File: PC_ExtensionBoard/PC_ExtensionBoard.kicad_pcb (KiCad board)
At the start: 2 copper layers, 135 x 125 mm, 2 parts, among them CN1 QT002206-4131-3H, CN2 QT002206-4131-3H

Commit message: update 3d
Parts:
- added CN3: HYC70-HDMIA19-230, DatCao_FootPrint:HDMI-TH_HYC70-HDMIA19-230, B.Cu at (89.5, 65.8)
- added DC1: DC-044A-20A, DatCao_FootPrint:DC-IN-TH_DC-044A-20A, B.Cu at (162.2, 56.8)
- added RJ1: 936273608, DatCao_FootPrint:RJ45-TH_936273608, B.Cu at (71.5, 64.0)
- added USB1: HC-USB3.0-L257-J, DatCao_FootPrint:USB-A-TH_HC-USB3.0-L257-J, B.Cu at (54.0, 68.6)
- added USB2: HC-USB2.0-L195-P, DatCao_FootPrint:USB-TH_73725-0110BLF, B.Cu at (99.2, 65.0)
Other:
- board size 135 x 125 mm -> 128.2 x 98.2 mm

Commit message: update footprint with 3D
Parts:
- removed CN3: HYC70-HDMIA19-230, DatCao_FootPrint:HDMI-TH_HYC70-HDMIA19-230
- removed USB2: HC-USB2.0-L195-P, DatCao_FootPrint:USB-TH_73725-0110BLF
- added HDMI1: HDMI-019S, ACLAB:HDMI-SMD_HDMI-019S, B.Cu at (107.5, 56.6)
- added PJ1: PJ-327A, ACLAB:AUDIO-IN-SMD_PJ-327A_C22355751, B.Cu at (164.3, 140.2)
- added U1: HC-USB3.0-L168-WP, ACLAB:USB-TH_USB3.0-A, B.Cu at (70.5, 62.1)
- added U2: 10GHz, ACLAB:SMA-TH_SMA-KWE, B.Cu at (56.5, 54.1)
- added USBC1: TYPE-C-31-M-12, ACLAB:USB-C_SMD-TYPE-C-31-M-12_1, B.Cu at (151.5, 141.5)
- CN1, CN2: footprint DatCao_FootPrint:CORE_BOARD_220PIN_Female -> ACLAB:CONN-SMD_QT002206-4131-3H
- DC1: footprint DatCao_FootPrint:DC-IN-TH_DC-044A-20A -> ACLAB:DC-IN-TH_DC-044A-20A
- RJ1: value 936273608 -> DS1128-09-S8B8S; footprint DatCao_FootPrint:RJ45-TH_936273608 -> ACLAB:RJ45-TH_DS1128-09-S8B8S
- USB1: value HC-USB3.0-L257-J -> HC-USB3.0-L175-2X1-P; footprint DatCao_FootPrint:USB-A-TH_HC-USB3.0-L257-J -> ACLAB:USB-A-TH_H181-AF2R06-12ALCR
- moved RJ1 56.4 mm to (127.8, 60.0), turned to 0 degrees
- moved USB1 36.3 mm to (89.5, 61.2)
- moved DC1 2.62 mm to (164.4, 55.3)

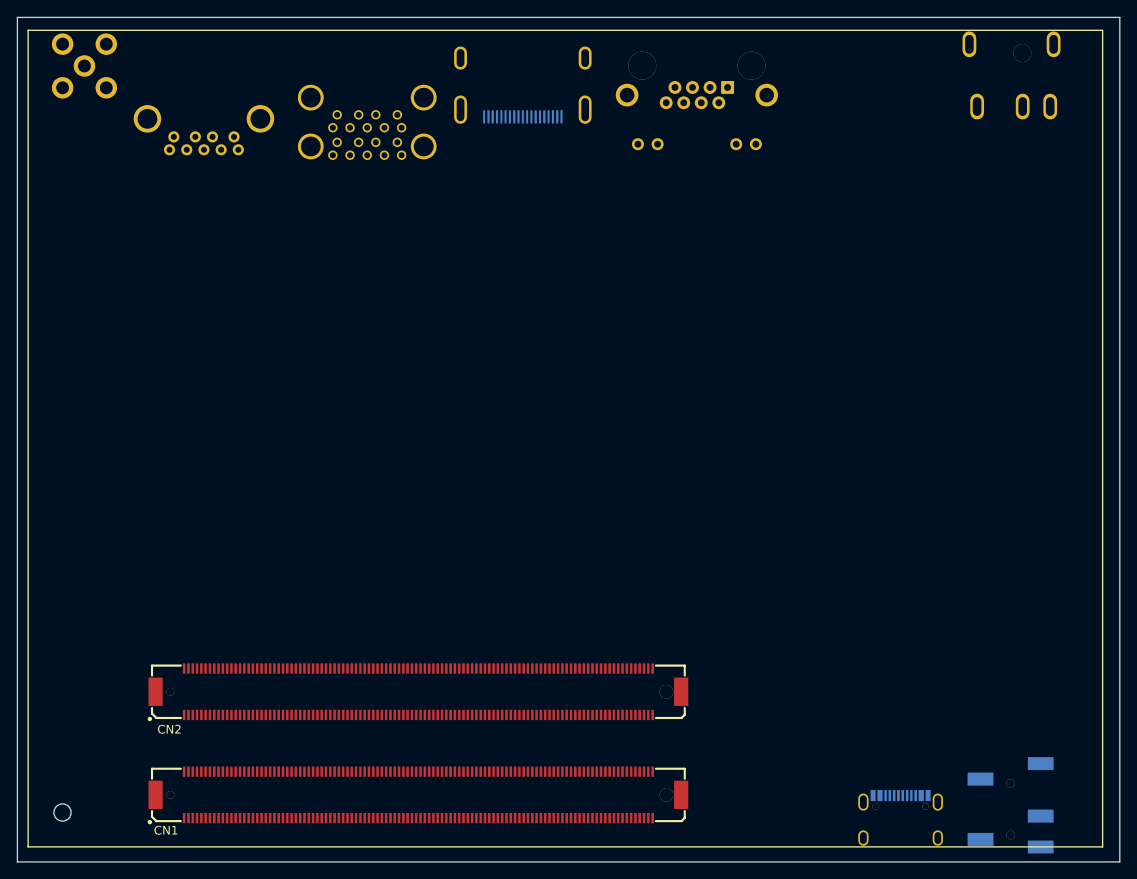
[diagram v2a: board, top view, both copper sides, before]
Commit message: finish 3D file for integration
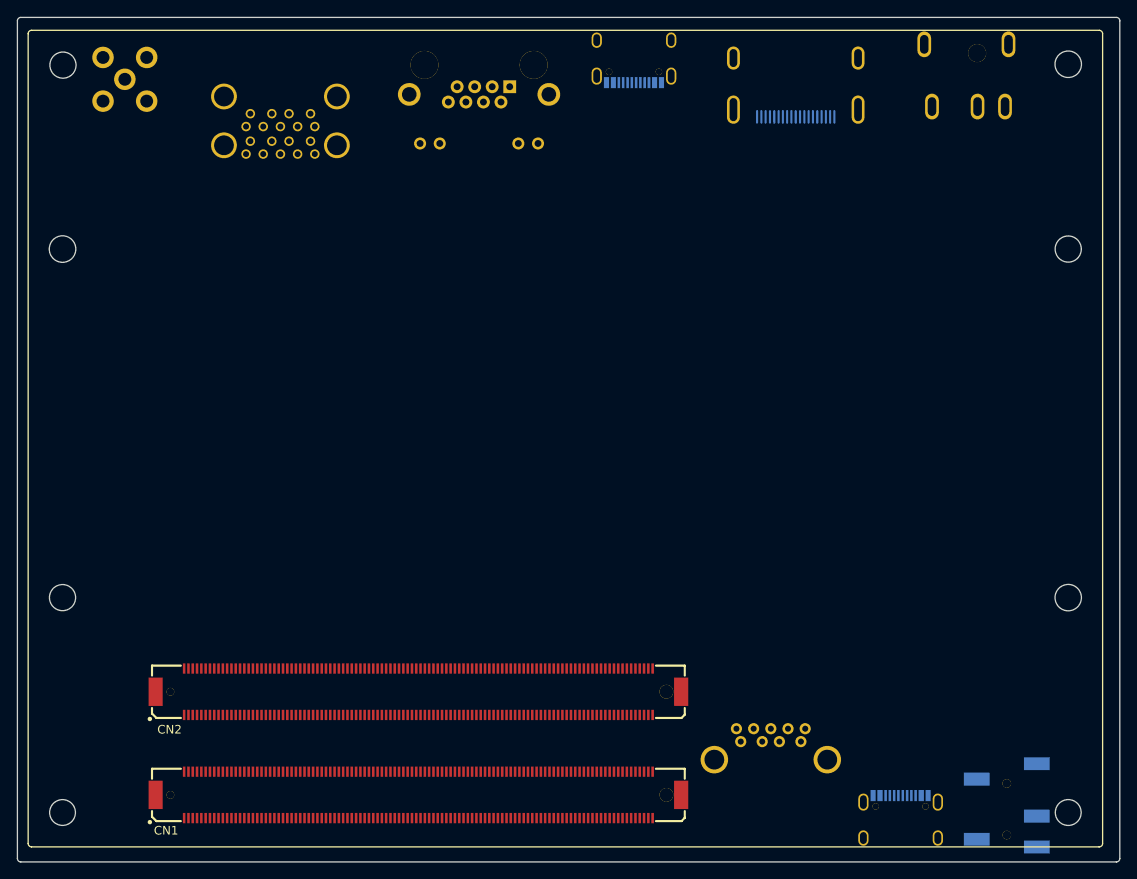
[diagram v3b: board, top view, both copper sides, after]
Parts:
- added USBC1: TYPE-C-31-M-12, ACLAB:USB-C_SMD-TYPE-C-31-M-12_1, B.Cu at (120.5, 53.6)
- moved U1 96.9 mm to (136.4, 133.1), turned to 180 degrees
- moved HDMI1 31.8 mm to (139.3, 56.6)
- moved RJ1 25.3 mm to (102.5, 59.9)
- moved USB1 10.1 mm to (79.3, 61.0)
- moved DC1 5.25 mm to (159.2, 55.3)
- moved U2 4.95 mm to (61.2, 55.7)
- moved PJ1 0.45 mm to (163.8, 140.2)
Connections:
- U1 pad 1: unconnected-(U1-VBUS-Pad1) -> (no net)
- U1 pad 10: unconnected-(U1-SH-Pad10) -> (no net)
- U1 pad 2: unconnected-(U1-D--Pad2) -> (no net)
- U1 pad 3: unconnected-(U1-D+-Pad3) -> (no net)
- U1 pad 4: unconnected-(U1-GND-Pad4) -> (no net)
- U1 pad 5: unconnected-(U1-SSRX--Pad5) -> (no net)
- U1 pad 6: unconnected-(U1-SSRX+-Pad6) -> (no net)
- U1 pad 7: unconnected-(U1-GND_DRAN-Pad7) -> (no net)
- U1 pad 8: unconnected-(U1-SSTX--Pad8) -> (no net)
- U1 pad 9: unconnected-(U1-SSTX+-Pad9) -> (no net)
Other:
- outline, holes or cut-outs redrawn

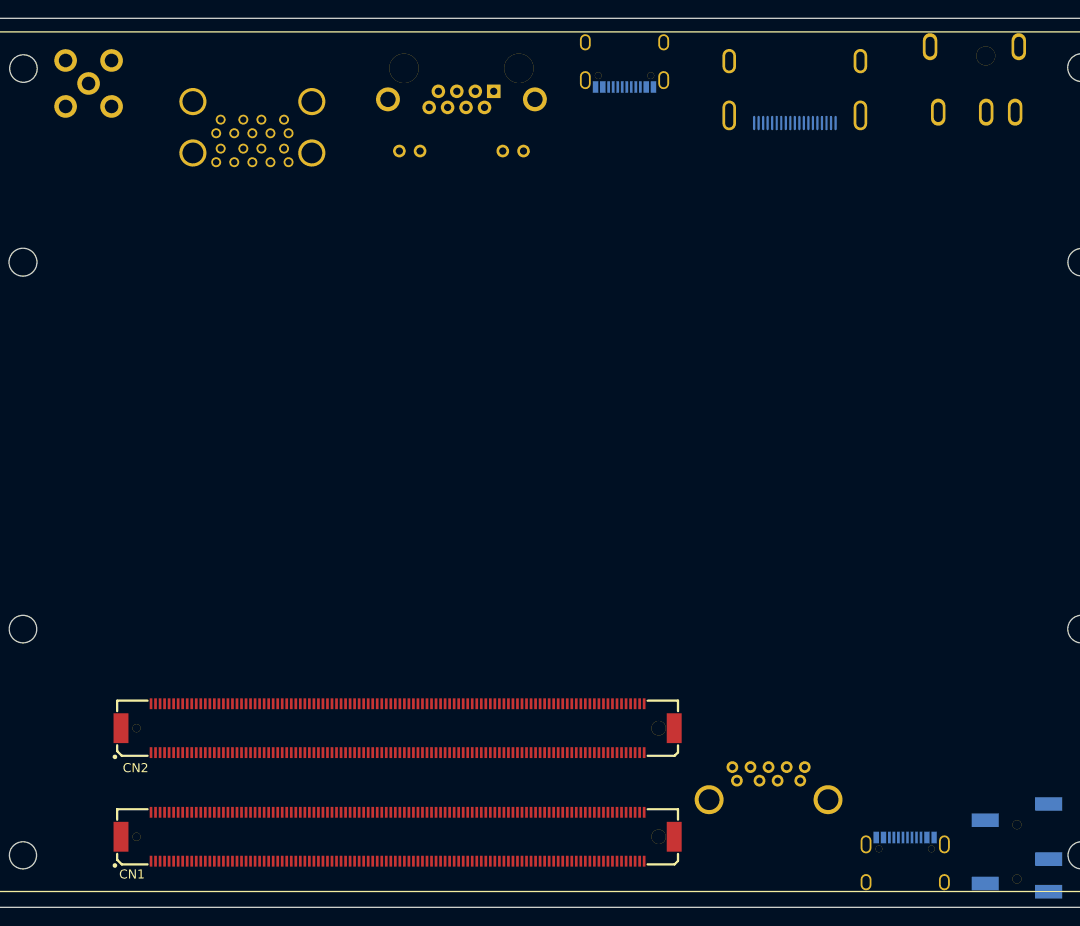
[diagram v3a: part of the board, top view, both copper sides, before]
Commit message: Update Symbol for Coreboard
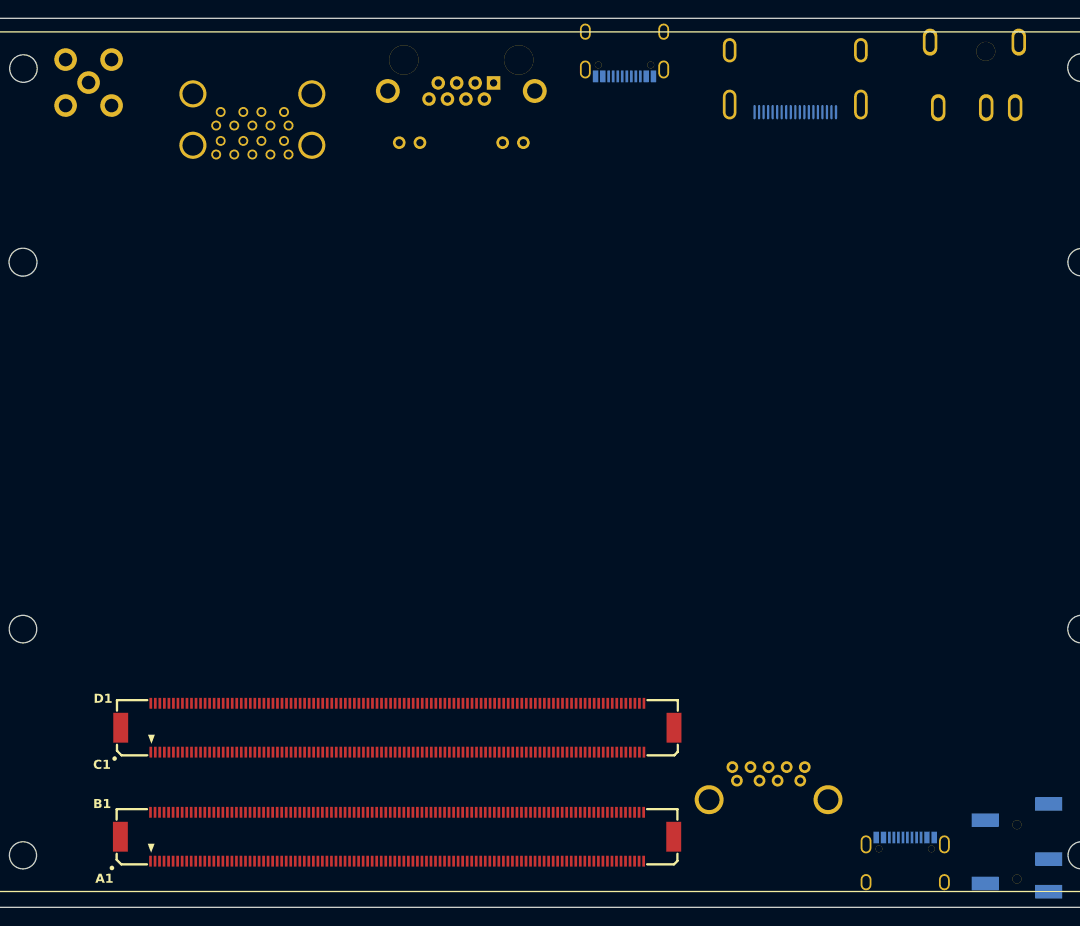
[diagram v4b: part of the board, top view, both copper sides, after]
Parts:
- removed CN1, CN2: QT002206-4131-3H, ACLAB:CONN-SMD_QT002206-4131-3H
- added U3: KBLH-E61_COMe_Type6_16U, DatCao_FootPrint:CORE_BOARD_CUSTOM_440_PIN, F.Cu at (95.3, 134.0)
- moved HDMI1 1.20 mm to (139.3, 55.5)
- moved USBC2 1.18 mm to (120.5, 52.4)
- moved RJ1 0.92 mm to (102.4, 58.9)
- moved USB1 0.85 mm to (79.3, 60.2)
- moved DC1 0.50 mm to (159.2, 54.8)
- moved U2 0.10 mm to (61.2, 55.6)
- renumbered USBC1 to USBC2
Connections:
- U1 pad 1: (no net) -> unconnected-(U1-VBUS-Pad1)
- U1 pad 10: (no net) -> unconnected-(U1-SH-Pad10)
- U1 pad 2: (no net) -> unconnected-(U1-D--Pad2)
- U1 pad 3: (no net) -> unconnected-(U1-D+-Pad3)
- U1 pad 4: (no net) -> unconnected-(U1-GND-Pad4)
- U1 pad 5: (no net) -> unconnected-(U1-SSRX--Pad5)
- U1 pad 6: (no net) -> unconnected-(U1-SSRX+-Pad6)
- U1 pad 7: (no net) -> unconnected-(U1-GND_DRAN-Pad7)
- U1 pad 8: (no net) -> unconnected-(U1-SSTX--Pad8)
- U1 pad 9: (no net) -> unconnected-(U1-SSTX+-Pad9)
- USB1 pad 1: unconnected-(USB1-VBUS-Pad1) -> /USB_Audio/P1_VBUS
- USB1 pad 10: unconnected-(USB1-VBUS-Pad10) -> /USB_Audio/P0_VBUS
- USB1 pad 11: unconnected-(USB1-D--Pad11) -> /USB_Audio/P0_D+
- USB1 pad 12: unconnected-(USB1-D+-Pad12) -> /USB_Audio/P0_D-
- USB1 pad 13: unconnected-(USB1-GND-Pad13) -> GND
- USB1 pad 14: unconnected-(USB1-SSRX--Pad14) -> /PC_CoreBoard/USBSS0.RX-
- USB1 pad 15: unconnected-(USB1-SSRX+-Pad15) -> /PC_CoreBoard/USBSS0.RX+
- USB1 pad 17: unconnected-(USB1-SSTX--Pad17) -> /PC_CoreBoard/USBSS0.TX-
- USB1 pad 18: unconnected-(USB1-SSTX+-Pad18) -> /PC_CoreBoard/USBSS0.TX+
- USB1 pad 19: unconnected-(USB1-GND-Pad19) -> GND
- USB1 pad 2: unconnected-(USB1-D--Pad2) -> /USB_Audio/P1_D+
- USB1 pad 20: unconnected-(USB1-GND-Pad20) -> GND
- USB1 pad 3: unconnected-(USB1-D+-Pad3) -> /USB_Audio/P1_D-
- USB1 pad 4: unconnected-(USB1-GND-Pad4) -> GND
- USB1 pad 5: unconnected-(USB1-SSRX--Pad5) -> /PC_CoreBoard/USBSS1.RX-
- USB1 pad 6: unconnected-(USB1-SSRX+-Pad6) -> /PC_CoreBoard/USBSS1.RX+
- USB1 pad 8: unconnected-(USB1-SSTX--Pad8) -> /PC_CoreBoard/USBSS1.TX-
- USB1 pad 9: unconnected-(USB1-SSTX+-Pad9) -> /PC_CoreBoard/USBSS1.TX+
- USBC2 pad 1: (no net) -> unconnected-(USBC2-EH-Pad1)
- USBC2 pad 2: (no net) -> unconnected-(USBC2-EH-Pad2)
- USBC2 pad 3: (no net) -> unconnected-(USBC2-EH-Pad3)
- USBC2 pad 4: (no net) -> unconnected-(USBC2-EH-Pad4)
- USBC2 pad A1B12: (no net) -> unconnected-(USBC2-GND-PadA1B12)
- USBC2 pad A4B9: (no net) -> unconnected-(USBC2-VBUS-PadA4B9)
- USBC2 pad A5: (no net) -> unconnected-(USBC2-CC1-PadA5)
- USBC2 pad A6: (no net) -> unconnected-(USBC2-DP1-PadA6)
- USBC2 pad A7: (no net) -> unconnected-(USBC2-DN1-PadA7)
- USBC2 pad A8: (no net) -> unconnected-(USBC2-SBU1-PadA8)
- USBC2 pad B1A12: (no net) -> unconnected-(USBC2-GND-PadB1A12)
- USBC2 pad B4A9: (no net) -> unconnected-(USBC2-VBUS-PadB4A9)
- USBC2 pad B5: (no net) -> unconnected-(USBC2-CC2-PadB5)
- USBC2 pad B6: (no net) -> unconnected-(USBC2-DP2-PadB6)
- USBC2 pad B7: (no net) -> unconnected-(USBC2-DN2-PadB7)
- USBC2 pad B8: (no net) -> unconnected-(USBC2-SBU2-PadB8)

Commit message: update schematic: add pattern
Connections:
- U3 pad C6: /PC_CoreBoard/USBSS1.RX- -> GND
- U3 pad C7: /PC_CoreBoard/USBSS1.RX+ -> GND
- U3 pad D6: /PC_CoreBoard/USBSS1.TX- -> GND
- U3 pad D7: /PC_CoreBoard/USBSS1.TX+ -> GND
- USB1 pad 1: /USB_Audio/P1_VBUS -> GND
- USB1 pad 10: /USB_Audio/P0_VBUS -> /PC_CoreBoard/USBSS0.TX+
- USB1 pad 11: /USB_Audio/P0_D+ -> /PC_CoreBoard/USBSS0.TX-
- USB1 pad 12: /USB_Audio/P0_D- -> unconnected-(USB1B-D+-Pad12)
- USB1 pad 13: GND -> /PC_CoreBoard/USBSS0.RX+
- USB1 pad 15: /PC_CoreBoard/USBSS0.RX+ -> GND
- USB1 pad 16: unconnected-(USB1-GND_DRAIN-Pad16) -> /USB_Audio/P0_D-
- USB1 pad 17: /PC_CoreBoard/USBSS0.TX- -> /USB_Audio/P0_D+
- USB1 pad 18: /PC_CoreBoard/USBSS0.TX+ -> /USB_Audio/P0_VBUS
- USB1 pad 19: GND -> unconnected-(USB1A-GND-Pad19)
- USB1 pad 2: /USB_Audio/P1_D+ -> GND
- USB1 pad 20: GND -> unconnected-(USB1B-GND-Pad20)
- USB1 pad 3: /USB_Audio/P1_D- -> GND
- USB1 pad 5: /PC_CoreBoard/USBSS1.RX- -> GND
- USB1 pad 6: /PC_CoreBoard/USBSS1.RX+ -> GND
- USB1 pad 7: unconnected-(USB1-GND_DRAIN-Pad7) -> /USB_Audio/P1_D-
- USB1 pad 8: /PC_CoreBoard/USBSS1.TX- -> /USB_Audio/P1_D+
- USB1 pad 9: /PC_CoreBoard/USBSS1.TX+ -> /USB_Audio/P1_VBUS
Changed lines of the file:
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@@
 			(size 0.3 1.2)
 			(layers "F.Cu" "F.Mask" "F.Paste")
-			(net "/PC_CoreBoard/USBSS1.RX-")
+			(net "GND")
 			(pinfunction "USB_SSRX1-_C6")
 			(pintype "input")
@@
 			(size 0.3 1.2)
 			(layers "F.Cu" "F.Mask" "F.Paste")
-			(net "/PC_CoreBoard/USBSS1.RX+")
+			(net "GND")
 			(pinfunction "USB_SSRX1+_C7")
 			(pintype "input")
@@
 			(size 0.3 1.2)
 			(layers "F.Cu" "F.Mask" "F.Paste")
-			(net "/PC_CoreBoard/USBSS1.TX-")
+			(net "GND")
 			(pinfunction "USB_SSTX1-_D6")
 			(pintype "output")
@@
 			(size 0.3 1.2)
 			(layers "F.Cu" "F.Mask" "F.Paste")
-			(net "/PC_CoreBoard/USBSS1.TX+")
+			(net "GND")
 			(pinfunction "USB_SSTX1+_D7")
 			(pintype "output")
@@
 			(unit
 				(name "A")
-				(pins "9" "8" "7" "6" "5" "10" "4" "3" "2" "1")
+				(pins "1" "2" "3" "4" "5" "6" "7" "8" "9" "10")
 			)
 		)
@@
 			(unit
 				(name "A")
-				(pins "9" "10" "8" "11" "7" "12" "6" "13" "5" "14" "4" "15" "3" "16"
-					"2" "17" "1" "18" "19" "20"
-				)
+				(pins "1" "2" "3" "4" "5" "6" "7" "8" "9" "19")
+			)
+			(unit
+				(name "B")
+				(pins "10" "11" "12" "13" "14" "15" "16" "17" "18" "20")
 			)
 		)
@@
 			(layers "*.Cu" "*.Mask")
 			(remove_unused_layers no)
-			(net "/USB_Audio/P1_VBUS")
+			(net "GND")
 			(pinfunction "VBUS_1")
 			(pintype "passive")
@@
 			(layers "*.Cu" "*.Mask")
 			(remove_unused_layers no)
-			(net "/USB_Audio/P1_D+")
+			(net "GND")
 			(pinfunction "D-_2")
 			(pintype "passive")
@@
 			(layers "*.Cu" "*.Mask")
 			(remove_unused_layers no)
-			(net "/USB_Audio/P1_D-")
+			(net "GND")
 			(pinfunction "D+_3")
 			(pintype "passive")
@@
 			(layers "*.Cu" "*.Mask")
 			(remove_unused_layers no)
-			(net "/PC_CoreBoard/USBSS1.RX-")
+			(net "GND")
 			(pinfunction "SSRX-_5")
 			(pintype "passive")
@@
 			(layers "*.Cu" "*.Mask")
 			(remove_unused_layers no)
-			(net "/PC_CoreBoard/USBSS1.RX+")
+			(net "GND")
 			(pinfunction "SSRX+_6")
 			(pintype "passive")
@@
 			(layers "*.Cu" "*.Mask")
 			(remove_unused_layers no)
-			(net "unconnected-(USB1-GND_DRAIN-Pad7)")
+			(net "/USB_Audio/P1_D-")
 			(pinfunction "GND_DRAIN_7")
 			(pintype "passive")
@@
 			(layers "*.Cu" "*.Mask")
 			(remove_unused_layers no)
-			(net "/PC_CoreBoard/USBSS1.TX-")
+			(net "/USB_Audio/P1_D+")
 			(pinfunction "SSTX-_8")
 			(pintype "passive")
@@
 			(layers "*.Cu" "*.Mask")
 			(remove_unused_layers no)
-			(net "/PC_CoreBoard/USBSS1.TX+")
+			(net "/USB_Audio/P1_VBUS")
 			(pinfunction "SSTX+_9")
 			(pintype "passive")
@@
 			(layers "*.Cu" "*.Mask")
 			(remove_unused_layers no)
-			(net "/USB_Audio/P0_VBUS")
+			(net "/PC_CoreBoard/USBSS0.TX+")
 			(pinfunction "VBUS_10")
 			(pintype "passive")
@@
 			(layers "*.Cu" "*.Mask")
 			(remove_unused_layers no)
-			(net "/USB_Audio/P0_D+")
+			(net "/PC_CoreBoard/USBSS0.TX-")
 			(pinfunction "D-_11")
 			(pintype "passive")
@@
 			(layers "*.Cu" "*.Mask")
 			(remove_unused_layers no)
-			(net "/USB_Audio/P0_D-")
+			(net "unconnected-(USB1B-D+-Pad12)")
 			(pinfunction "D+_12")
 			(pintype "passive")
@@
 			(layers "*.Cu" "*.Mask")
 			(remove_unused_layers no)
-			(net "GND")
+			(net "/PC_CoreBoard/USBSS0.RX+")
 			(pinfunction "GND_13")
 			(pintype "passive")
@@
 			(layers "*.Cu" "*.Mask")
 			(remove_unused_layers no)
-			(net "/PC_CoreBoard/USBSS0.RX+")
+			(net "GND")
 			(pinfunction "SSRX+_15")
 			(pintype "passive")
@@
 			(layers "*.Cu" "*.Mask")
 			(remove_unused_layers no)
-			(net "unconnected-(USB1-GND_DRAIN-Pad16)")
+			(net "/USB_Audio/P0_D-")
 			(pinfunction "GND_DRAIN_16")
 			(pintype "passive")
@@
 			(layers "*.Cu" "*.Mask")
 			(remove_unused_layers no)
-			(net "/PC_CoreBoard/USBSS0.TX-")
+			(net "/USB_Audio/P0_D+")
 			(pinfunction "SSTX-_17")
 			(pintype "passive")
@@
 			(layers "*.Cu" "*.Mask")
 			(remove_unused_layers no)
-			(net "/PC_CoreBoard/USBSS0.TX+")
+			(net "/USB_Audio/P0_VBUS")
 			(pinfunction "SSTX+_18")
 			(pintype "passive")
@@
 			(layers "*.Cu" "*.Mask")
 			(remove_unused_layers no)
-			(net "GND")
+			(net "unconnected-(USB1A-GND-Pad19)")
 			(pinfunction "GND_19")
 			(pintype "passive")
@@
 			(layers "*.Cu" "*.Mask")
 			(remove_unused_layers no)
-			(net "GND")
+			(net "unconnected-(USB1A-GND-Pad19)")
 			(pinfunction "GND_19")
 			(pintype "passive")
@@
 			(layers "*.Cu" "*.Mask")
 			(remove_unused_layers no)
-			(net "GND")
+			(net "unconnected-(USB1B-GND-Pad20)")
 			(pinfunction "GND_20")
 			(pintype "passive")
@@
 			(layers "*.Cu" "*.Mask")
 			(remove_unused_layers no)
-			(net "GND")
+			(net "unconnected-(USB1B-GND-Pad20)")
 			(pinfunction "GND_20")
 			(pintype "passive")
